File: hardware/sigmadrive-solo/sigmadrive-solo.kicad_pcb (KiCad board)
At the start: 4 copper layers, 70.7 x 87.3 mm, 163 parts, among them J1 CONN_01X02, J10 Conn_01x03, J11 Conn_01x03, J12 Conn_01x05, J2 CONN_02X05, J3 CONN_01X03, J4 Conn_01x03, J5 Conn_01x05, J6 629_105_150_921, J7 CONN_01X02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

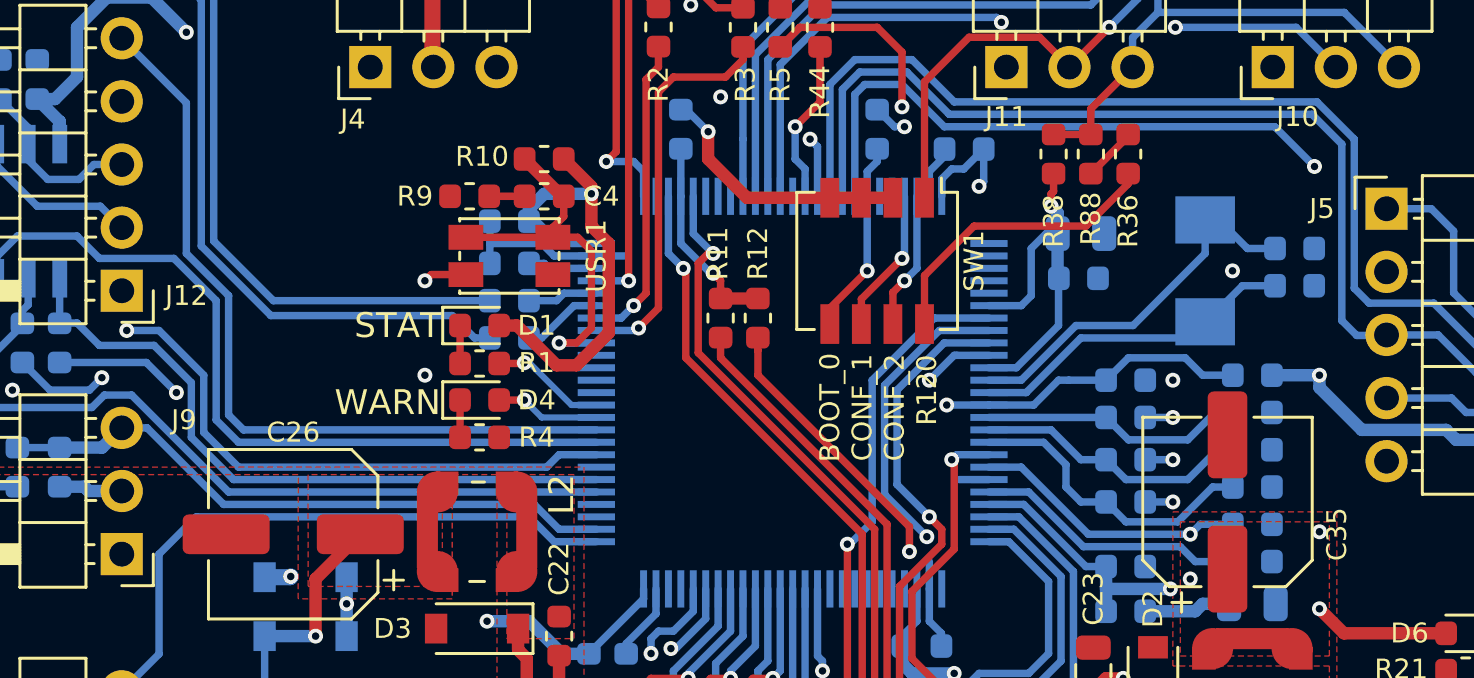
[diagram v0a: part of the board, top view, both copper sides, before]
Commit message: Added ground via between the two MCU clock capacitors.
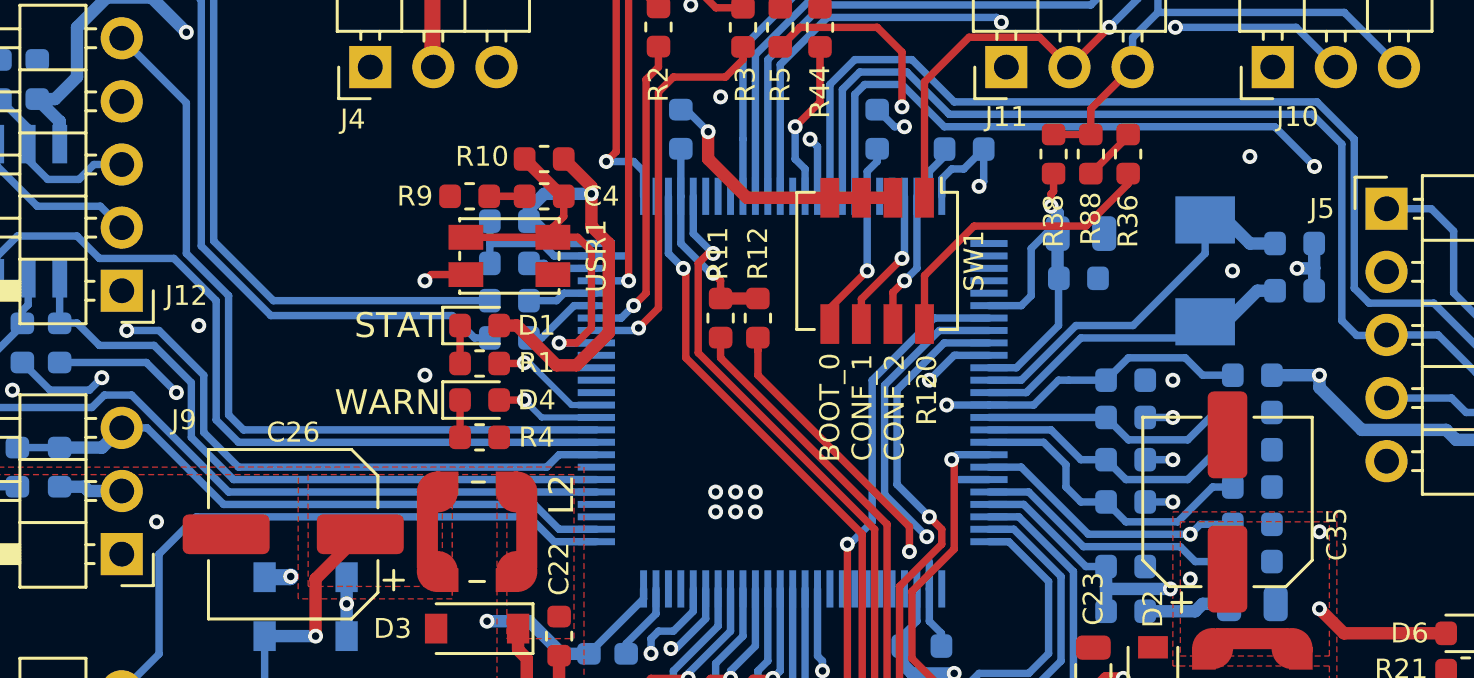
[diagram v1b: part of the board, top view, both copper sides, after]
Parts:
- moved C27 0.20 mm to (133.6, 48.9)
- moved C32 0.20 mm to (133.6, 50.8)
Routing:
- net GND: track 89.5 -> 92.1 mm, vias 22 -> 32
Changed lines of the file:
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@@
     (thickness 1.6)
     (drawings 23)
-    (tracks 1522)
+    (tracks 1536)
     (zones 0)
     (modules 163)
@@
     (0 F.Cu mixed)
     (1 In1.Cu mixed)
-    (2 In2.Cu mixed)
+    (2 In2.Cu mixed hide)
     (31 B.Cu mixed)
     (32 B.Adhes user hide)
@@
   )
   (module Capacitor_SMD:C_0603_1608Metric (layer B.Cu)
-    (at 133.6 49.1)
+    (at 133.6 48.9)
     (descr "Capacitor SMD 0603 (1608 Metric), square (rectangular) end terminal, IPC_7351 nominal, (Body size source: http://www.tortai-tech.com/upload/download/2011102023233369053.pdf), generated with kicad-footprint-generator")
     (tags capacitor)
@@
   )
   (module Capacitor_SMD:C_0603_1608Metric (layer B.Cu)
-    (at 133.6 50.6)
+    (at 133.6 50.8)
     (descr "Capacitor SMD 0603 (1608 Metric), square (rectangular) end terminal, IPC_7351 nominal, (Body size source: http://www.tortai-tech.com/upload/download/2011102023233369053.pdf), generated with kicad-footprint-generator")
     (tags capacitor)
@@
   (segment (start 126.3 70.4) (end 127.8 71.9) (width 0.5) (layer F.Cu) (net 4))
   (via (at 129.4 62.4) (size 0.6) (drill 0.3) (layers F.Cu B.Cu) (net 4))
+  (via (at 133.7 49.9) (size 0.6) (drill 0.3) (layers F.Cu B.Cu) (net 4))
+  (segment (start 134.375 49.9) (end 134.3875 49.8875) (width 0.5) (layer B.Cu) (net 4))
+  (segment (start 133.7 49.9) (end 134.375 49.9) (width 0.5) (layer B.Cu) (net 4))
+  (segment (start 134.3875 48.9) (end 134.3875 49.8875) (width 0.5) (layer B.Cu) (net 4))
+  (segment (start 134.3875 49.8875) (end 134.3875 50.8) (width 0.5) (layer B.Cu) (net 4))
+  (via (at 131.8 45.4) (size 0.6) (drill 0.3) (layers F.Cu B.Cu) (net 4))
+  (via (at 110.3 59.7) (size 0.6) (drill 0.3) (layers F.Cu B.Cu) (net 4))
+  (via (at 111.1 59.7) (size 0.6) (drill 0.3) (layers F.Cu B.Cu) (net 4))
+  (via (at 111.9 59.7) (size 0.6) (drill 0.3) (layers F.Cu B.Cu) (net 4))
+  (via (at 111.9 58.9) (size 0.6) (drill 0.3) (layers F.Cu B.Cu) (net 4))
+  (via (at 111.1 58.9) (size 0.6) (drill 0.3) (layers F.Cu B.Cu) (net 4))
+  (via (at 110.3 58.9) (size 0.6) (drill 0.3) (layers F.Cu B.Cu) (net 4))
+  (via (at 87.8 60.1) (size 0.6) (drill 0.3) (layers F.Cu B.Cu) (net 4))
+  (via (at 89.5 52.2) (size 0.6) (drill 0.3) (layers F.Cu B.Cu) (net 4))
   (segment (start 102.6 55.2) (end 101.5875 55.2) (width 0.3) (layer F.Cu) (net 5))
   (via (at 102.6 55.2) (size 0.6) (drill 0.3) (layers F.Cu B.Cu) (net 5))
@@
   (segment (start 130 47.95) (end 130 49.3) (width 0.3) (layer B.Cu) (net 24))
   (segment (start 130 49.3) (end 127.1 52.2) (width 0.3) (layer B.Cu) (net 24))
-  (segment (start 130.55 47.95) (end 130 47.95) (width 0.3) (layer B.Cu) (net 24))
-  (segment (start 132.8125 49.1) (end 131.7 49.1) (width 0.3) (layer B.Cu) (net 24))
-  (segment (start 131.7 49.1) (end 130.55 47.95) (width 0.3) (layer B.Cu) (net 24))
+  (segment (start 130 47.95) (end 130.85 47.95) (width 0.5) (layer B.Cu) (net 24))
+  (segment (start 131.8 48.9) (end 132.8125 48.9) (width 0.5) (layer B.Cu) (net 24))
+  (segment (start 130.85 47.95) (end 131.8 48.9) (width 0.5) (layer B.Cu) (net 24))
   (segment (start 131.1125 61.7) (end 131.1125 62.2875) (width 0.3) (layer B.Cu) (net 25))
   (segment (start 130.9625 62.4375) (end 130.9625 63.4) (width 0.3) (layer B.Cu) (net 25))
@@
   (segment (start 121.3 54.9) (end 122.8 54.9) (width 0.3) (layer B.Cu) (net 26))
   (segment (start 122.8 54.9) (end 125 52.7) (width 0.3) (layer B.Cu) (net 26))
-  (segment (start 130.05 52.05) (end 130 52.05) (width 0.3) (layer B.Cu) (net 26))
-  (segment (start 132.8125 50.6) (end 131.5 50.6) (width 0.3) (layer B.Cu) (net 26))
-  (segment (start 131.5 50.6) (end 130.05 52.05) (width 0.3) (layer B.Cu) (net 26))
+  (segment (start 130 52.05) (end 130.85 52.05) (width 0.5) (layer B.Cu) (net 26))
+  (segment (start 132.1 50.8) (end 132.8125 50.8) (width 0.5) (layer B.Cu) (net 26))
+  (segment (start 130.85 52.05) (end 132.1 50.8) (width 0.5) (layer B.Cu) (net 26))
   (segment (start 100.013097 52.2) (end 100.013097 53.727913) (width 0.3) (layer F.Cu) (net 27))
   (segment (start 100.0125 55.2) (end 100.0125 56.7) (width 0.3) (layer F.Cu) (net 28))

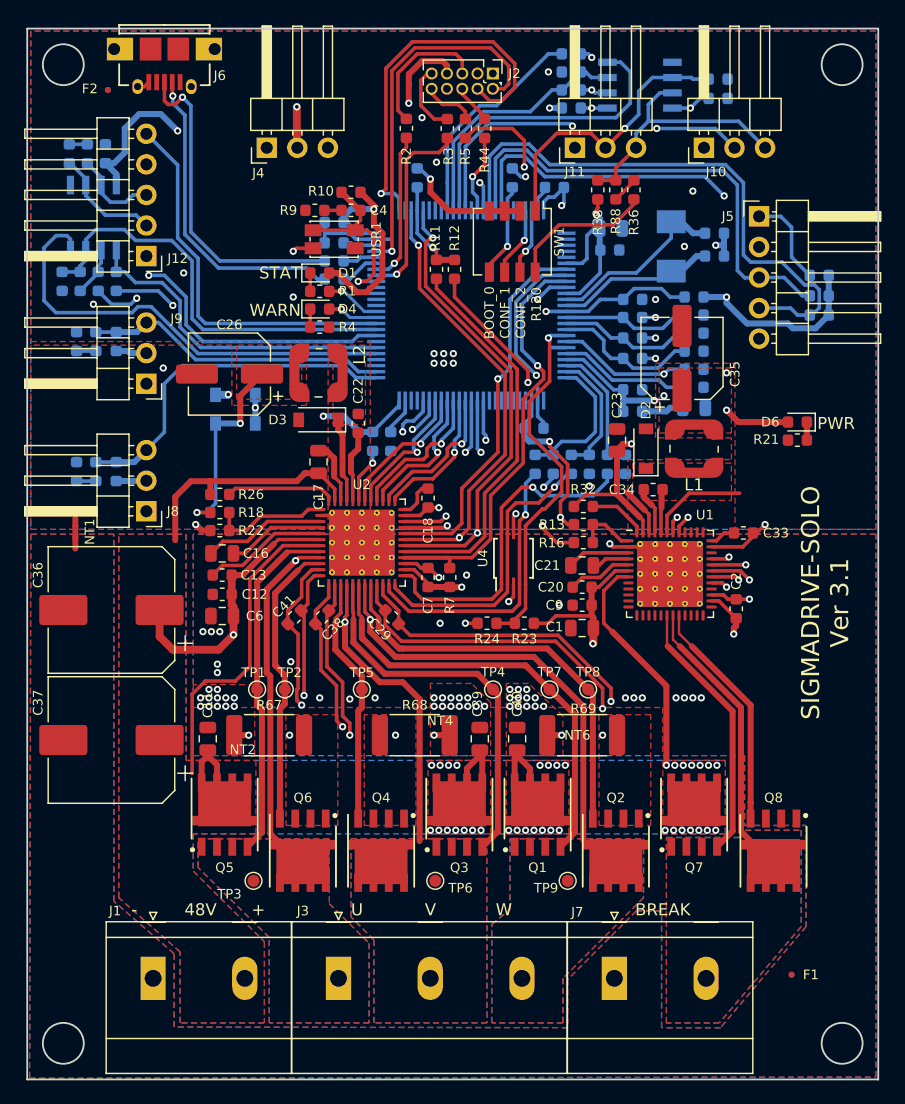
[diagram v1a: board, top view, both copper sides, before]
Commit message: Changed MCU to STM32F745
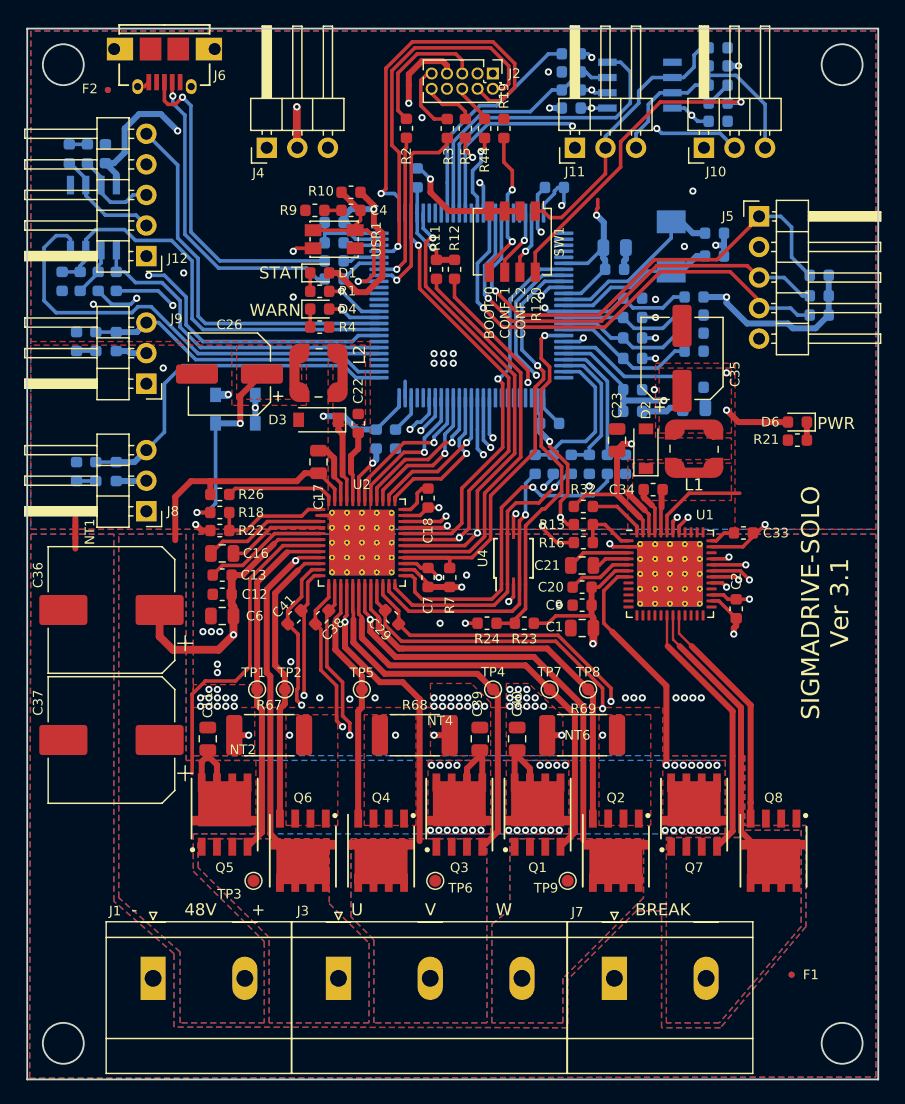
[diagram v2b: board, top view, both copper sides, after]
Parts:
- removed C25: 100nF 50V, Capacitor_SMD:C_0603_1608Metric
- R19: moved to F.Cu
- R36, R38, R88: moved to B.Cu
- U5: value STM32F405VGTx -> STM32F745VETx
- moved R38 14.4 mm to (133.9, 35.0), turned to 0 degrees
- moved R88 12.2 mm to (133.9, 36.6), turned to 0 degrees
- moved R36 10.0 mm to (133.9, 38.1), turned to 0 degrees
- moved R19 4.16 mm to (116.1, 40.2)
- moved R40 2.60 mm to (133.9, 33.5)
- moved C8 1.90 mm to (133.9, 39.6)
- moved C54 1.65 mm to (125.3, 51.9)
- moved C28 1.63 mm to (125.3, 50.1)
- moved C24 1.36 mm to (119.9, 64.7)
- moved C10 0.45 mm to (107.1, 66.0)
- moved C19 0.36 mm to (105.5, 66.0)
- moved C3 0.10 mm to (126.8, 54.3)
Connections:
- U5 pad 19: +3V3 -> GND
- U5 pad 20: GND -> Net-(C30-Pad1)
- U5 pad 21: Net-(C30-Pad1) -> +3V3
- U5 pad 22: +3V3 -> /MCU/PA0
- U5 pad 23: /MCU/PA0 -> /MCU/PA1
- U5 pad 24: /MCU/PA1 -> /MCU/PA2
- U5 pad 25: /MCU/PA2 -> /MCU/PA3
- U5 pad 26: /MCU/PA3 -> GND
- U5 pad 27: GND -> +3V3
- U5 pad 28: +3V3 -> /MCU/PA4
- U5 pad 29: /MCU/PA4 -> /MCU/PA5
- U5 pad 30: /MCU/PA5 -> /MCU/PA6
- U5 pad 31: /MCU/PA6 -> /MCU/PA7
- U5 pad 32: /MCU/PA7 -> /MCU/PC4
- U5 pad 33: /MCU/PC4 -> /MCU/PC5
- U5 pad 34: /MCU/PC5 -> /MCU/PB0
- U5 pad 35: /MCU/PB0 -> /MCU/GATE2_ENABLE
- U5 pad 36: /MCU/GATE2_ENABLE -> /MCU/AUX_H
- U5 pad 37: /MCU/AUX_H -> /MCU/AUX_L
- U5 pad 38: /MCU/AUX_L -> /MCU/PWM_AL
- U5 pad 39: /MCU/PWM_AL -> /MCU/PWM_AH
- U5 pad 40: /MCU/PWM_AH -> /MCU/PWM_BL
- U5 pad 41: /MCU/PWM_BL -> /MCU/PWM_BH
- U5 pad 42: /MCU/PWM_BH -> /MCU/PWM_CL
- U5 pad 43: /MCU/PWM_CL -> /MCU/PWM_CH
- U5 pad 44: /MCU/PWM_CH -> /MCU/GATE_ENABLE
- U5 pad 45: /MCU/GATE_ENABLE -> /MCU/DRV_CAL
- U5 pad 46: /MCU/DRV_CAL -> /MCU/PB10
- U5 pad 47: /MCU/PB10 -> /MCU/PB11
- U5 pad 48: /MCU/PB11 -> Net-(C10-Pad2)
- U5 pad 49: Net-(C10-Pad2) -> GND
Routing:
- net /MCU/B_TERM_R120: track 12.1 -> 26.3 mm, vias 0 -> 1
- net /MCU/ENCODER_Z: track 47.8 -> 40.0 mm, vias 0 -> 1
- net +3V3: track 340.0 -> 334.5 mm
- net /MCU/ENCODER_B: track 35.4 -> 40.8 mm
- net /MCU/BOOT0: track 7.84 -> 12.6 mm, vias 1 -> 2
- net Net-(C3-Pad2): track 33.7 -> 30.0 mm
- net GND: track 92.1 -> 94.2 mm
- net /MCU/A_TERM_R120: track 33.7 -> 35.8 mm, vias 2 -> 1
- net /MCU/ENCODER_A: track 39.9 -> 38.0 mm, vias 0 -> 1
- net Net-(J10-Pad3): track 21.9 -> 20.6 mm
- net /MCU/PWM_AH: track 11.5 -> 12.8 mm
- net /MCU/PWM_CL: track 11.9 -> 12.9 mm
- net +5V: track 196.9 -> 197.9 mm
- net /MCU/PA1: track 10.6 -> 11.6 mm
- net /MCU/PA0: track 11.0 -> 12.0 mm
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
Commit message: Added DIR and BUSY lines.
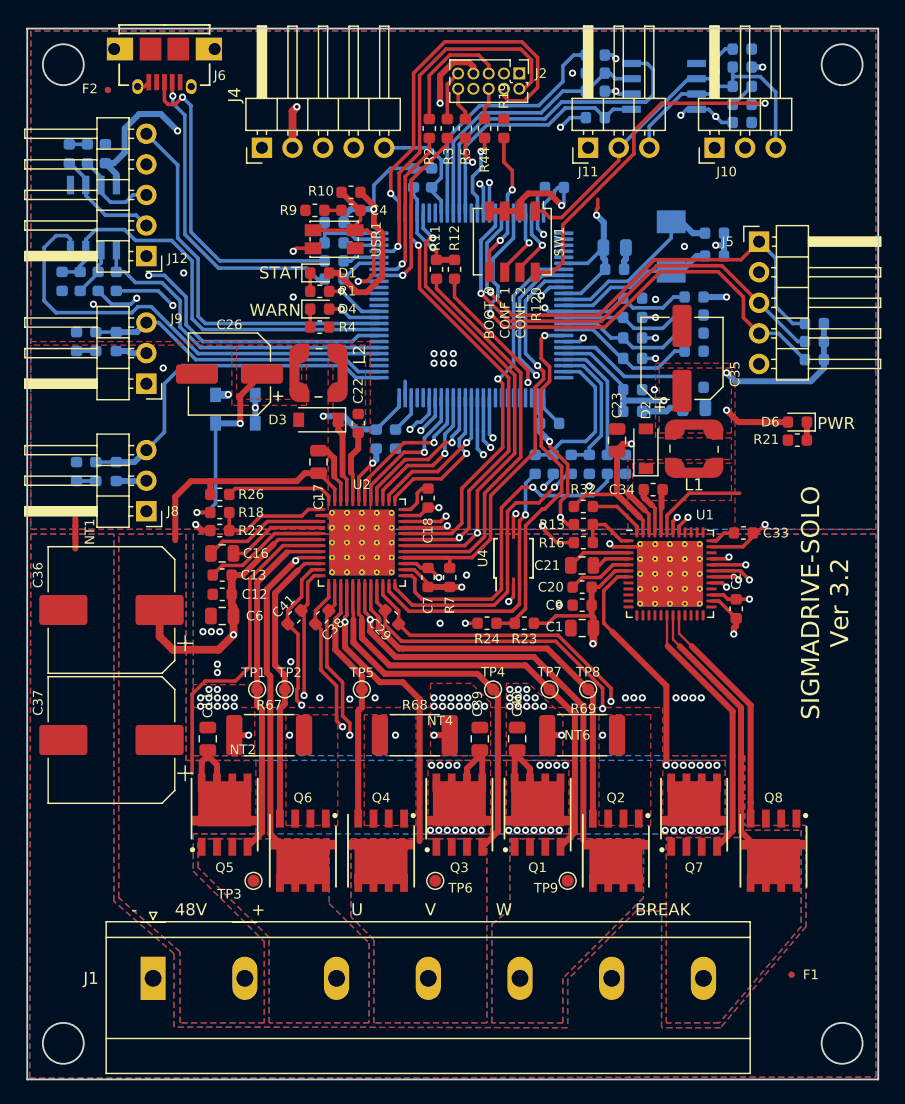
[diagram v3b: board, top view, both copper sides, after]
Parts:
- removed J3: CONN_01X03, Sigmadrone:PhoenixContact_MKDS_03x7.62mm_Vertical
- removed J7: CONN_01X02, Sigmadrone:PhoenixContact_MKDS_02x7.62mm_Vertical
- added R37: 10k, Resistor_SMD:R_0603_1608Metric, B.Cu at (110.1, 44.3)
- J1: footprint Sigmadrone:PhoenixContact_MKDS_02x7.62mm_Vertical -> Sigmadrone:PhoenixContact_MKDS_07x7.62mm_Vertical
- J4: value Conn_01x03 -> Conn_01x05; footprint Connector_PinHeader_2.54mm:PinHeader_1x03_P2.54mm_Horizontal -> Connector_PinHeader_2.54mm:PinHeader_1x05_P2.54mm_Horizontal
- moved R92 4.02 mm to (141.9, 56.4)
- moved R91 3.82 mm to (141.9, 57.9)
- moved R90 3.72 mm to (141.9, 59.4)
- moved J2 2.20 mm to (117.4, 35.6)
- moved R84 2.15 mm to (123.7, 39.3)
- moved J5 2.10 mm to (137.3, 49.6)
- moved C8 2.00 mm to (135.9, 39.7)
- moved R34 2.00 mm to (123.7, 34.1)
- moved R35 2.00 mm to (123.7, 37.1)
- moved R36 2.00 mm to (135.9, 38.2)
- moved R38 2.00 mm to (135.9, 35.1)
- moved R40 2.00 mm to (135.9, 33.6)
- moved R85 2.00 mm to (123.7, 35.6)
- moved R88 2.00 mm to (135.9, 36.7)
- moved U12 2.00 mm to (129.4, 36.7)
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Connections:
- U5 pad 83: /MCU/PD2 -> /MCU/BUSY
- U5 pad 91: /MCU/ENCODER_Z -> /MCU/DIR
- U5 pad 95: /MCU/PB8 -> /MCU/ENCODER_Z
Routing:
- net /MCU/DIR: track 0.00 -> 15.7 mm, vias 0 -> 1
- net /MCU/BUSY: track 0.00 -> 10.2 mm
- net +3V3: track 334.5 -> 340.5 mm
- net /MCU/A_TERM_R120: track 35.8 -> 30.8 mm
- net /MCU/PD3: track 18.6 -> 21.4 mm
- net /MCU/B_TERM_R120: track 26.3 -> 29.0 mm
- net /MCU/ENCODER_Z: track 40.0 -> 42.6 mm
- net /MCU/EXT_5V: track 53.5 -> 55.5 mm
- net /MCU/PD4: track 21.3 -> 23.2 mm
- net Net-(J2-Pad9): track 5.90 -> 4.16 mm
- net /MCU/NRST: track 4.43 -> 2.76 mm
- net /MCU/PD6: track 19.7 -> 21.3 mm, vias 2 -> 0
- net /MCU/ENCODER_A: track 38.0 -> 39.6 mm
- net /MCU/PA9: track 16.4 -> 14.9 mm
- net /MCU/PD5: track 26.2 -> 27.6 mm
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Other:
- board text added: "SIGMADRIVE-SOLO Ver 3.2"
- board text removed: "SIGMADRIVE-SOLO Ver 3.1"
